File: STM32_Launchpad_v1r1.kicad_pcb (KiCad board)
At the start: 4 copper layers, 54 x 75 mm, 61 parts, among them J1 Conn_01x04, J2 USB_B_Micro, J3 Conn_02x10_Counter_Clockwise, J4 Conn_01x02, J5 Conn_02x10_Counter_Clockwise, J6 Conn_01x03, J7 Conn_02x03_Odd_Even, J8 Conn_01x02, SW1 SW_Push, U1 TPD2EUSB30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

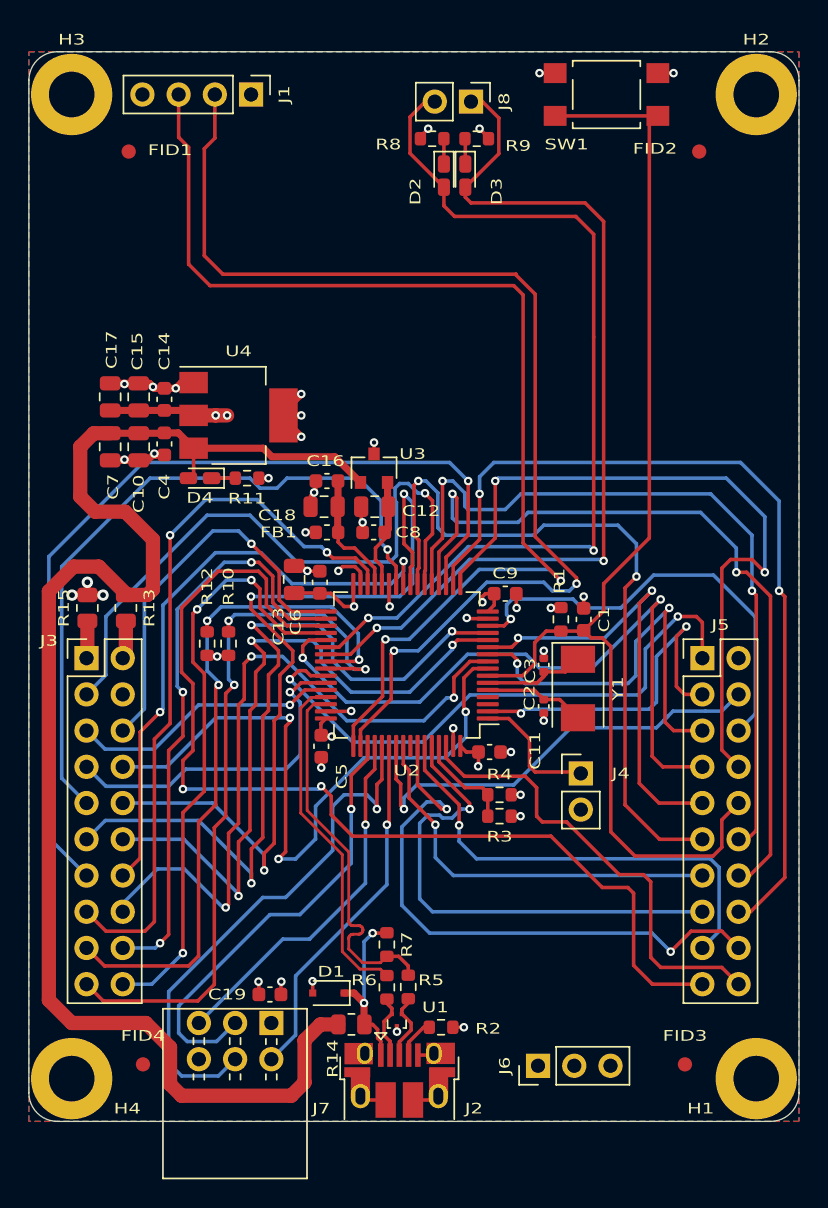
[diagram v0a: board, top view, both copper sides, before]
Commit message: Added stitching vias
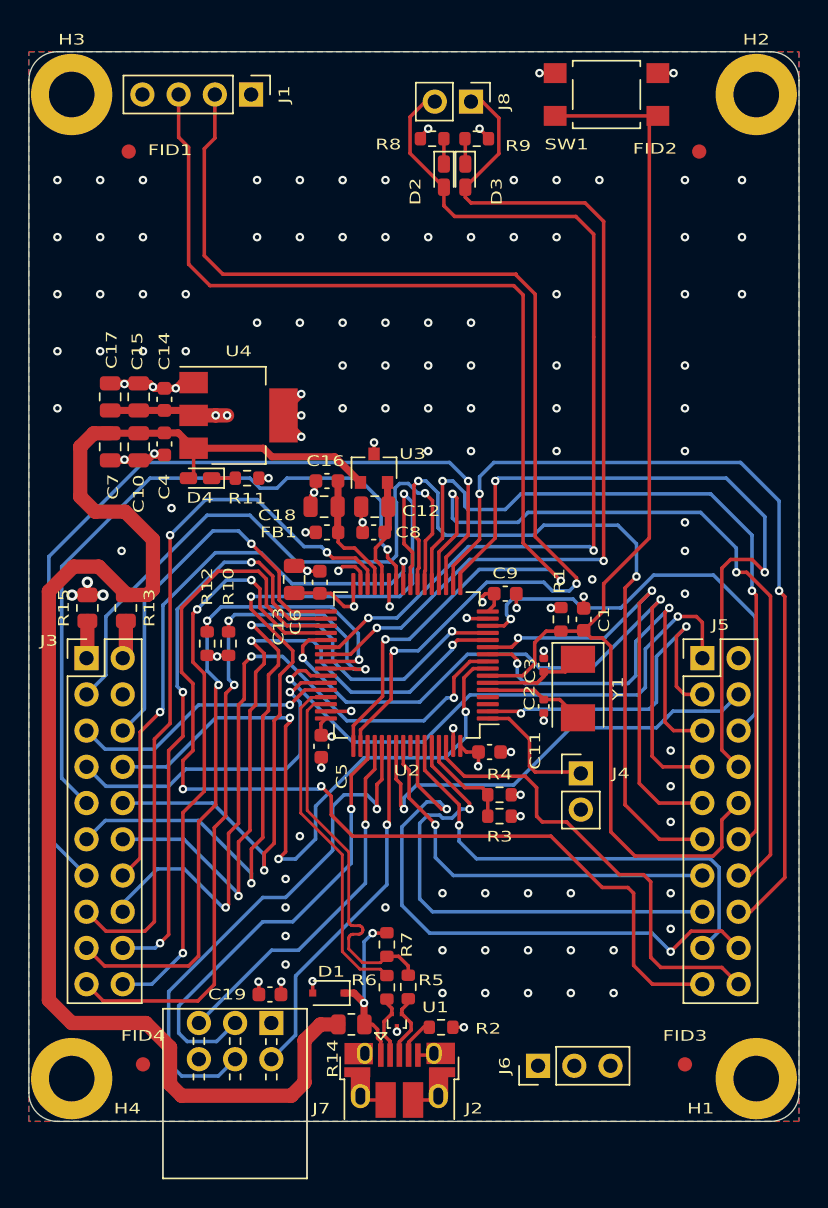
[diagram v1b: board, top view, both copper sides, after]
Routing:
- net GND: vias 30 -> 120
